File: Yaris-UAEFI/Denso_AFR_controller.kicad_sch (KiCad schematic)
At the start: 34 parts, among them Q1 NPN, Q2 PNP, Q3 NPN, Q4 PNP, U3 MCP6024T-I-ST

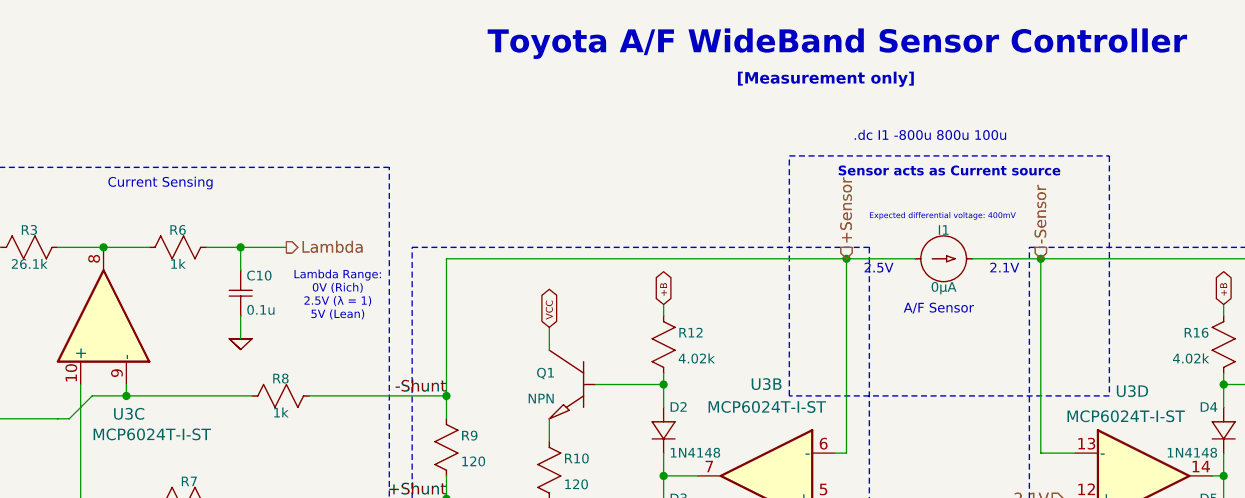
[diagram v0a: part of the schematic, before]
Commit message: Fix LPF R value
wrong LPF resistor on lambda output
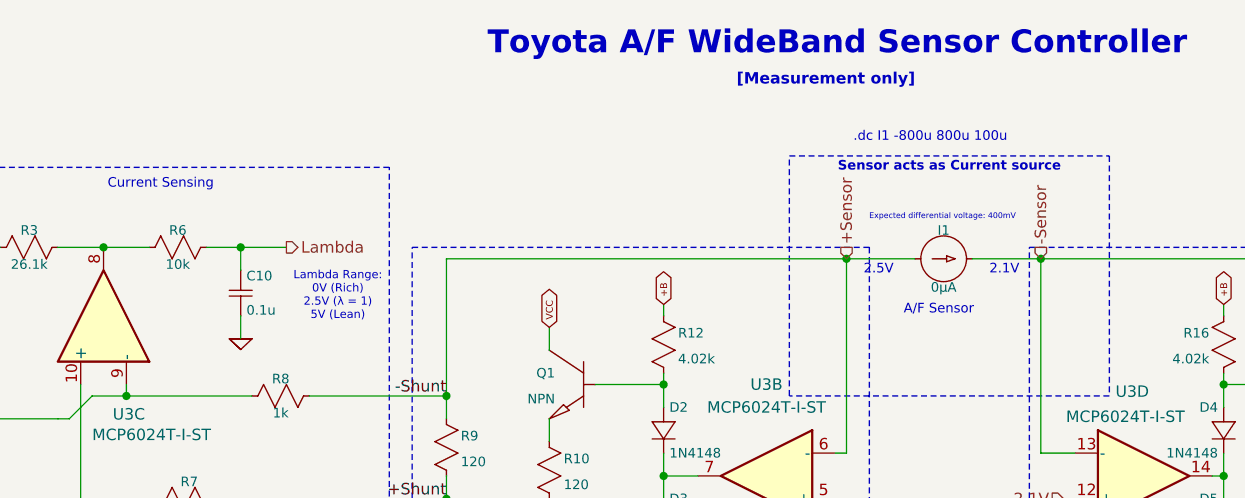
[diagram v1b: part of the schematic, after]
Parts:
- R6: value 1k -> 10k
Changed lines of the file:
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@@
 	(text "Sensor acts as Current source"
 		(exclude_from_sim no)
-		(at 165.1 64.135 0)
+		(at 165.1 63.5 0)
 		(effects
 			(font
@@
 		(at 83.82 71.12 270)
 		(unit 1)
-		(body_style 0)
+		(body_style 1)
 		(exclude_from_sim no)
 		(in_bom yes)
@@
 			)
 		)
-		(property "Value" "1k"
+		(property "Value" "10k"
 			(at 79.375 73.66 90)
 			(show_name no)

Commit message: Fix Q2,Q4 pinout
Fix transistor pinout same as LTspice and multisim
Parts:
- R7: value 1k -> 10k
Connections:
- net 0: now also Q2.1 (C), Q4.1 (C); no longer Q2.3 (E), Q4.3 (E)
- net at R11.2: now also Q2.3 (E); no longer Q2.1 (C)
- net at R19.2: now also Q4.3 (E); no longer Q4.1 (C)
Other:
- moved on the sheet: Q2
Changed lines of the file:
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@@
 	(wire
 		(pts
-			(xy 208.28 114.3) (xy 208.28 111.76)
-		)
-		(stroke
-			(width 0.1524)
-			(type solid)
-		)
-	)
-	(wire
-		(pts
 			(xy 234.95 109.22) (xy 234.95 119.38)
 		)
@@
 	(wire
 		(pts
-			(xy 120.65 114.3) (xy 120.65 111.76)
+			(xy 208.28 111.76) (xy 208.28 114.3)
 		)
 		(stroke
-			(width 0.1524)
-			(type solid)
+			(width 0)
+			(type default)
 		)
 	)
@@
 	(wire
 		(pts
+			(xy 120.65 111.76) (xy 120.65 114.3)
+		)
+		(stroke
+			(width 0)
+			(type default)
+		)
+	)
+	(wire
+		(pts
 			(xy 218.44 111.76) (xy 218.44 114.3)
 		)
@@
 	(symbol
 		(lib_id "ltspice:pnp")
-		(at 125.73 114.3 0)
-		(mirror y)
+		(at 125.73 121.92 180)
 		(unit 1)
 		(body_style 0)
@@
 		(dnp no)
 		(property "Reference" "Q2"
-			(at 119.0498 116.84 0)
+			(at 119.0498 119.38 0)
 			(show_name no)
 			(do_not_autoplace no)
@@
 		)
 		(property "Value" "PNP"
-			(at 119.0498 119.7102 0)
+			(at 119.0498 116.5098 0)
 			(show_name no)
 			(do_not_autoplace no)
@@
 		)
 		(property "Footprint" ""
-			(at 125.73 114.3 0)
+			(at 125.73 121.92 0)
 			(hide yes)
 			(show_name no)
@@
 		)
 		(property "Datasheet" ""
-			(at 125.73 114.3 0)
+			(at 125.73 121.92 0)
 			(hide yes)
 			(show_name no)
@@
 		)
 		(property "Description" ""
-			(at 125.73 114.3 0)
+			(at 125.73 121.92 0)
 			(hide yes)
 			(show_name no)
@@
 		)
 		(property "Sim.Library" "C:\\Users\\Ram\\AppData\\Local\\LTspice\\lib\\cmp/standard.bjt"
-			(at 125.73 114.3 0)
+			(at 125.73 121.92 0)
 			(hide yes)
 			(show_name no)
@@
 		)
 		(property "Sim.Name" "PNP"
-			(at 125.73 114.3 0)
+			(at 125.73 121.92 0)
 			(hide yes)
 			(show_name no)
@@
 		)
 		(property "Sim.Device" "SPICE"
-			(at 125.73 114.3 0)
+			(at 125.73 121.92 0)
 			(hide yes)
 			(show_name no)
@@
 		)
 		(property "Sim.Params" "model=\"PNP\""
-			(at 125.73 114.3 0)
+			(at 125.73 121.92 0)
 			(hide yes)
 			(show_name no)
@@
 	(symbol
 		(lib_id "ltspice:pnp")
-		(at 203.2 114.3 0)
+		(at 203.2 121.92 0)
+		(mirror x)
 		(unit 1)
 		(body_style 0)
@@
 		(dnp no)
 		(property "Reference" "Q4"
-			(at 209.8802 116.84 0)
+			(at 209.8802 119.38 0)
 			(show_name no)
 			(do_not_autoplace no)
@@
 		)
 		(property "Value" "PNP"
-			(at 209.8802 119.7102 0)
+			(at 209.8802 116.5098 0)
 			(show_name no)
 			(do_not_autoplace no)
@@
 		)
 		(property "Footprint" ""
-			(at 203.2 114.3 0)
+			(at 203.2 121.92 0)
 			(hide yes)
 			(show_name no)
@@
 		)
 		(property "Datasheet" ""
-			(at 203.2 114.3 0)
+			(at 203.2 121.92 0)
 			(hide yes)
 			(show_name no)
@@
 		)
 		(property "Description" ""
-			(at 203.2 114.3 0)
+			(at 203.2 121.92 0)
 			(hide yes)
 			(show_name no)
@@
 		)
 		(property "Sim.Library" "C:\\Users\\Ram\\AppData\\Local\\LTspice\\lib\\cmp/standard.bjt"
-			(at 203.2 114.3 0)
+			(at 203.2 121.92 0)
 			(hide yes)
 			(show_name no)
@@
 		)
 		(property "Sim.Name" "PNP"
-			(at 203.2 114.3 0)
+			(at 203.2 121.92 0)
 			(hide yes)
 			(show_name no)
@@
 		)
 		(property "Sim.Device" "SPICE"
-			(at 203.2 114.3 0)
+			(at 203.2 121.92 0)
 			(hide yes)
 			(show_name no)
@@
 		)
 		(property "Sim.Params" "model=\"PNP\""
-			(at 203.2 114.3 0)
+			(at 203.2 121.92 0)
 			(hide yes)
 			(show_name no)
@@
 			)
 		)
-		(property "Value" "1k"
+		(property "Value" "10k"
 			(at 80.645 101.6 90)
 			(show_name no)
